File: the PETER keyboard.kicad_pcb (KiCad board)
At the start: 2 copper layers, 241.6 x 96.9 mm, 141 parts, among them J1 USB_C_Receptacle_USB2.0, SW1 RotaryEncoder_Switch, SW12 RotaryEncoder_Switch, SW2 SW_Push, U1 ATmega32U4-M, Y1 Crystal_GND24_Small

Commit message: re doing the auto routing
having to start again
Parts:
- moved C_Decoupler3 4.07 mm to (154.7, 98.7)
- moved U1 1.37 mm to (150.2, 104.3), turned to 45 degrees
- moved C_Decoupler1 0.28 mm to (145.8, 96.9)
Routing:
- net GND: track 430.5 -> 0.00 mm
- net ROW0: track 309.4 -> 0.00 mm
- net ROW2: track 255.9 -> 0.00 mm, vias 2 -> 0
- net ROTARY_A: track 242.3 -> 0.00 mm
- net ROTARY_B: track 237.0 -> 0.00 mm
- net ROW4: track 217.1 -> 0.00 mm
- net ROW1: track 216.5 -> 0.00 mm, vias 2 -> 0
- net  ROW3: track 215.9 -> 0.00 mm
- net +5V: track 91.5 -> 0.00 mm
- net COL7: track 90.7 -> 0.00 mm
- net COL0: track 90.0 -> 0.00 mm
- net COL5: track 86.5 -> 0.00 mm
- net COL1: track 84.1 -> 0.00 mm
- net COL4: track 83.1 -> 0.00 mm
- net COL2: track 83.1 -> 0.00 mm
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
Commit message: back to autorouting
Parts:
- moved U1 0.46 mm to (149.9, 104.5), turned to 0 degrees
- moved C_Decoupler3 0.28 mm to (154.9, 98.6)
- turned C_Decoupler2 to 180 degrees
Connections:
- U1 pad 10: unconnected-(U1-Pad10) -> ROW2
- U1 pad 11: unconnected-(U1-Pad11) -> COL0
- U1 pad 12: unconnected-(U1-Pad12) -> COL1
- U1 pad 18: unconnected-(U1-Pad18) -> COL2
- U1 pad 19: unconnected-(U1-Pad19) -> COL3
- U1 pad 20: unconnected-(U1-Pad20) -> COL4
- U1 pad 21: unconnected-(U1-Pad21) -> COL5
- U1 pad 22: unconnected-(U1-Pad22) -> COL6
- U1 pad 25: unconnected-(U1-Pad25) -> COL7
- U1 pad 26: unconnected-(U1-Pad26) -> COL8
- U1 pad 27: unconnected-(U1-Pad27) -> COL9
- U1 pad 31: unconnected-(U1-Pad31) -> ROTARY_A
- U1 pad 32: unconnected-(U1-Pad32) -> ROTARY_B
- U1 pad 38: unconnected-(U1-Pad38) -> COL10
- U1 pad 39: unconnected-(U1-Pad39) -> COL11
- U1 pad 40: unconnected-(U1-Pad40) -> ROW4
- U1 pad 41: unconnected-(U1-Pad41) ->  ROW3
- U1 pad 8: unconnected-(U1-Pad8) -> ROW0
- U1 pad 9: unconnected-(U1-Pad9) -> ROW1
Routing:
- added copper zone on B.Cu, net GND
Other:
- board text added: "add the pcb cut outs for bottom mounting"

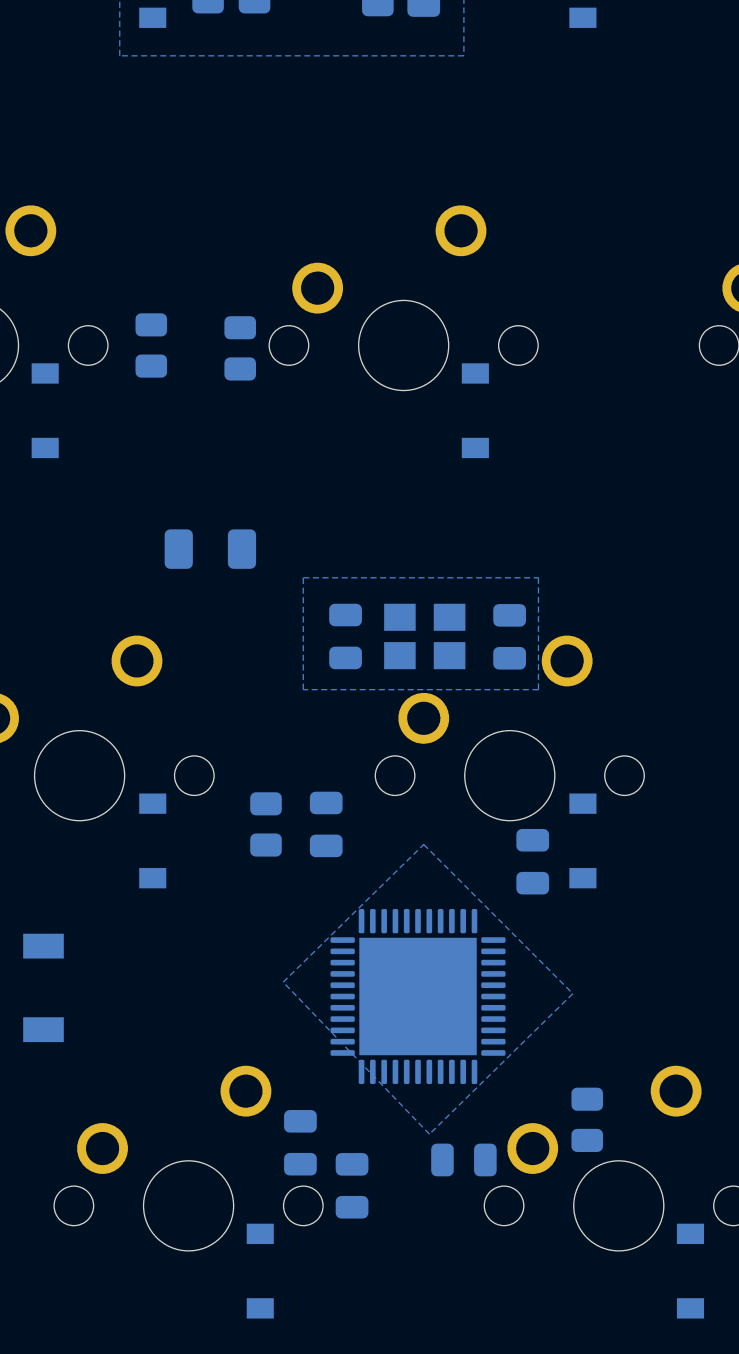
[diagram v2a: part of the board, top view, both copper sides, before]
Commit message: moving MCU around, no trace attempt yet
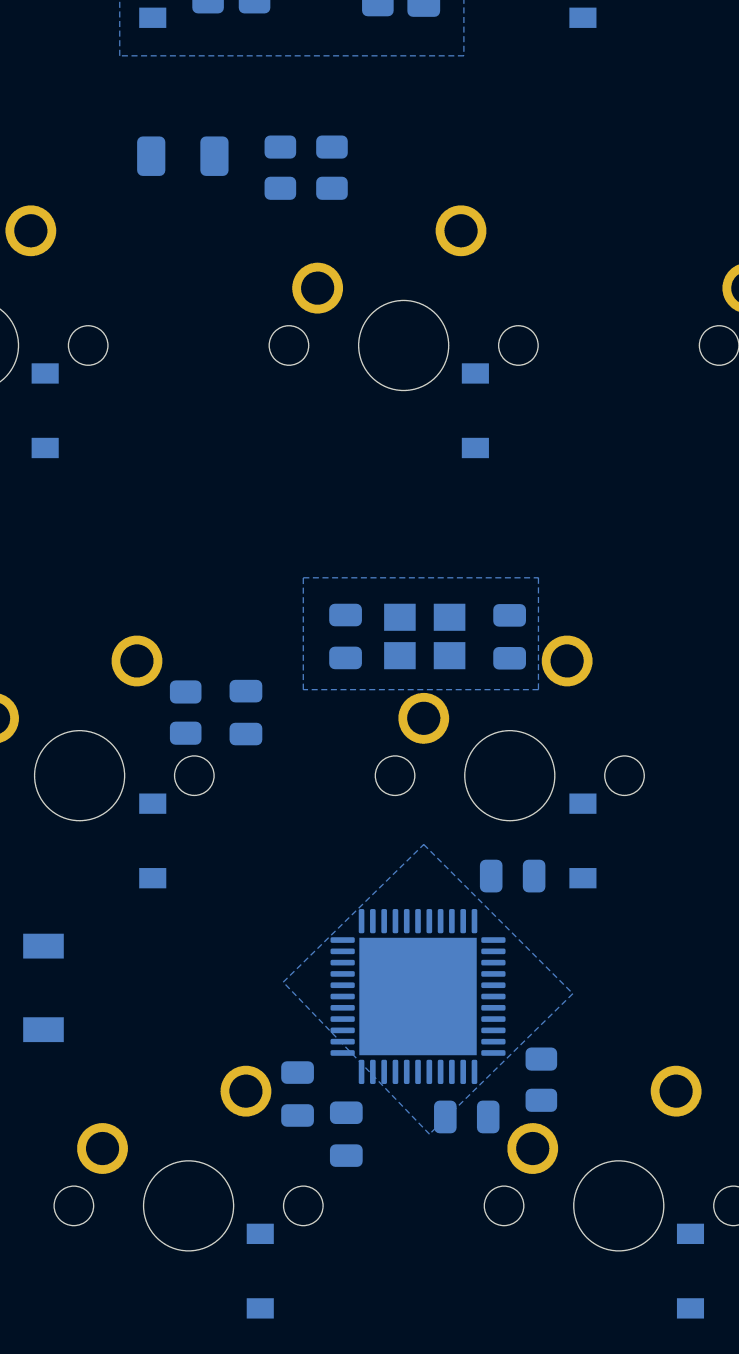
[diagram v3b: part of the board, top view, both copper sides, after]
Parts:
- moved F_USBC1 17.4 mm to (139.4, 67.3)
- moved R_USB3 9.73 mm to (143.8, 67.8)
- moved R_USB4 8.97 mm to (146.1, 67.8)
- moved C_Decoupler1 6.10 mm to (142.2, 91.9)
- moved R_reset1 6.10 mm to (139.6, 91.9)
- moved R_HWB/PE2 2.70 mm to (155.3, 108.2)
- moved C_Decoupler4 2.30 mm to (146.7, 110.6)
- moved C_UCAP1 2.16 mm to (144.5, 108.8)
- moved C_Decoupler2 1.91 mm to (152.0, 109.9)
- moved C_Decoupler3 1.09 mm to (154.1, 99.2), turned to 180 degrees
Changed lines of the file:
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@@
   )
   (footprint "Resistor_SMD:R_0805_2012Metric" (layer "B.Cu")
-    (at 143.129 96.901 -90)
+    (at 139.573 91.948 -90)
     (descr "Resistor SMD 0805 (2012 Metric), square (rectangular) end terminal, IPC_7351 nominal, (Body size source: IPC-SM-782 page 72, https://www.pcb-3d.com/wordpress/wp-content/uploads/ipc-sm-782a_amendment_1_and_2.pdf), generated with kicad-footprint-generator")
     (tags "resistor")
@@
   )
   (footprint "Resistor_SMD:R_0805_2012Metric" (layer "B.Cu")
-    (at 157.353 109.982 -90)
+    (at 155.321 108.204 -90)
     (descr "Resistor SMD 0805 (2012 Metric), square (rectangular) end terminal, IPC_7351 nominal, (Body size source: IPC-SM-782 page 72, https://www.pcb-3d.com/wordpress/wp-content/uploads/ipc-sm-782a_amendment_1_and_2.pdf), generated with kicad-footprint-generator")
     (tags "resistor")
@@
   )
   (footprint "Capacitor_SMD:C_0805_2012Metric" (layer "B.Cu")
-    (at 145.796 96.901 90)
+    (at 142.24 91.948 90)
     (descr "Capacitor SMD 0805 (2012 Metric), square (rectangular) end terminal, IPC_7351 nominal, (Body size source: IPC-SM-782 page 76, https://www.pcb-3d.com/wordpress/wp-content/uploads/ipc-sm-782a_amendment_1_and_2.pdf, https://docs.google.com/spreadsheets/d/1BsfQQcO9C6DZCsRaXUlFlo91Tg2WpOkGARC1WS5S8t0/edit?usp=sharing), generated with kicad-footprint-generator")
     (tags "capacitor")
@@
   )
   (footprint "Resistor_SMD:R_0805_2012Metric" (layer "B.Cu")
-    (at 138.049 75.692 -90)
+    (at 143.764 67.818 -90)
     (descr "Resistor SMD 0805 (2012 Metric), square (rectangular) end terminal, IPC_7351 nominal, (Body size source: IPC-SM-782 page 72, https://www.pcb-3d.com/wordpress/wp-content/uploads/ipc-sm-782a_amendment_1_and_2.pdf), generated with kicad-footprint-generator")
     (tags "resistor")
@@
   )
   (footprint "Capacitor_SMD:C_0805_2012Metric" (layer "B.Cu")
-    (at 151.892 111.76 180)
+    (at 152.019 109.855 180)
     (descr "Capacitor SMD 0805 (2012 Metric), square (rectangular) end terminal, IPC_7351 nominal, (Body size source: IPC-SM-782 page 76, https://www.pcb-3d.com/wordpress/wp-content/uploads/ipc-sm-782a_amendment_1_and_2.pdf, https://docs.google.com/spreadsheets/d/1BsfQQcO9C6DZCsRaXUlFlo91Tg2WpOkGARC1WS5S8t0/edit?usp=sharing), generated with kicad-footprint-generator")
     (tags "capacitor")
@@
   )
   (footprint "Resistor_SMD:R_0805_2012Metric" (layer "B.Cu")
-    (at 141.986 75.819 -90)
+    (at 146.05 67.818 -90)
     (descr "Resistor SMD 0805 (2012 Metric), square (rectangular) end terminal, IPC_7351 nominal, (Body size source: IPC-SM-782 page 72, https://www.pcb-3d.com/wordpress/wp-content/uploads/ipc-sm-782a_amendment_1_and_2.pdf), generated with kicad-footprint-generator")
     (tags "resistor")
@@
   )
   (footprint "Fuse:Fuse_1206_3216Metric" (layer "B.Cu")
-    (at 140.6652 84.709 180)
+    (at 139.446 67.31 180)
     (descr "Fuse SMD 1206 (3216 Metric), square (rectangular) end terminal, IPC_7351 nominal, (Body size source: http://www.tortai-tech.com/upload/download/2011102023233369053.pdf), generated with kicad-footprint-generator")
     (tags "fuse")
@@
   )
   (footprint "Capacitor_SMD:C_0805_2012Metric" (layer "B.Cu")
-    (at 144.653 110.998 -90)
+    (at 144.526 108.839 -90)
     (descr "Capacitor SMD 0805 (2012 Metric), square (rectangular) end terminal, IPC_7351 nominal, (Body size source: IPC-SM-782 page 76, https://www.pcb-3d.com/wordpress/wp-content/uploads/ipc-sm-782a_amendment_1_and_2.pdf, https://docs.google.com/spreadsheets/d/1BsfQQcO9C6DZCsRaXUlFlo91Tg2WpOkGARC1WS5S8t0/edit?usp=sharing), generated with kicad-footprint-generator")
     (tags "capacitor")
@@
   )
   (footprint "Capacitor_SMD:C_0805_2012Metric" (layer "B.Cu")
-    (at 146.939 112.903 -90)
+    (at 146.685 110.617 -90)
     (descr "Capacitor SMD 0805 (2012 Metric), square (rectangular) end terminal, IPC_7351 nominal, (Body size source: IPC-SM-782 page 76, https://www.pcb-3d.com/wordpress/wp-content/uploads/ipc-sm-782a_amendment_1_and_2.pdf, https://docs.google.com/spreadsheets/d/1BsfQQcO9C6DZCsRaXUlFlo91Tg2WpOkGARC1WS5S8t0/edit?usp=sharing), generated with kicad-footprint-generator")
     (tags "capacitor")
@@
   )
   (footprint "Capacitor_SMD:C_0805_2012Metric" (layer "B.Cu")
-    (at 154.94 98.552 90)
+    (at 154.051 99.187 180)
     (descr "Capacitor SMD 0805 (2012 Metric), square (rectangular) end terminal, IPC_7351 nominal, (Body size source: IPC-SM-782 page 76, https://www.pcb-3d.com/wordpress/wp-content/uploads/ipc-sm-782a_amendment_1_and_2.pdf, https://docs.google.com/spreadsheets/d/1BsfQQcO9C6DZCsRaXUlFlo91Tg2WpOkGARC1WS5S8t0/edit?usp=sharing), generated with kicad-footprint-generator")
     (tags "capacitor")
@@
     (property "Sheetname" "")
     (attr smd)
-    (fp_text reference "C_Decoupler3" (at 0 1.68 90) (layer "B.SilkS") hide
-      (effects (font (size 1 1) (thickness 0.15)) (justify mirror))
-    )
-    (fp_text value "0.1uF" (at 0 -1.68 90) (layer "B.Fab")
-      (effects (font (size 1 1) (thickness 0.15)) (justify mirror))
-    )
-    (fp_text user "${REFERENCE}" (at 0 0 90) (layer "B.Fab")
+    (fp_text reference "C_Decoupler3" (at 0 1.68) (layer "B.SilkS") hide
+      (effects (font (size 1 1) (thickness 0.15)) (justify mirror))
+    )
+    (fp_text value "0.1uF" (at 0 -1.68) (layer "B.Fab")
+      (effects (font (size 1 1) (thickness 0.15)) (justify mirror))
+    )
+    (fp_text user "${REFERENCE}" (at 0 0) (layer "B.Fab")
       (effects (font (size 0.5 0.5) (thickness 0.08)) (justify mirror))
     )
@@
     (fp_line (start 1 0.625) (end 1 -0.625) (layer "B.Fab") (width 0.1))
     (fp_line (start 1 -0.625) (end -1 -0.625) (layer "B.Fab") (width 0.1))
-    (pad "1" smd roundrect (at -0.95 0 90) (size 1 1.45) (layers "B.Cu" "B.Paste" "B.Mask") (roundrect_rratio 0.25)
+    (pad "1" smd roundrect (at -0.95 0 180) (size 1 1.45) (layers "B.Cu" "B.Paste" "B.Mask") (roundrect_rratio 0.25)
       (net 4 "+5V") (pintype "passive"))
-    (pad "2" smd roundrect (at 0.95 0 90) (size 1 1.45) (layers "B.Cu" "B.Paste" "B.Mask") (roundrect_rratio 0.25)
+    (pad "2" smd roundrect (at 0.95 0 180) (size 1 1.45) (layers "B.Cu" "B.Paste" "B.Mask") (roundrect_rratio 0.25)
       (net 1 "GND") (pintype "passive"))
     (model "${KICAD6_3DMODEL_DIR}/Capacitor_SMD.3dshapes/C_0805_2012Metric.wrl"

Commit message: just tried and deleted a silkscreen
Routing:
- removed copper zone on B.Cu, net GND
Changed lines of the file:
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@@
     (style (thickness 0.15) (arrow_length 1.27) (text_position_mode 0) (extension_height 0.58642) (extension_offset 0.5) keep_text_aligned)
   )
-  (zone (net 1) (net_name "GND") (layer "B.Cu") (hatch edge 0.508)
-    (connect_pads (clearance 0.508))
-    (min_thickness 0.254) (filled_areas_thickness no)
-    (fill yes (thermal_gap 0.508) (thermal_bridge_width 0.508))
-    (polygon
-      (pts
-        (xy 151.892 47.117)
-        (xy 151.892 62.865)
-        (xy 136.652 62.865)
-        (xy 136.652 46.99)
-      )
-    )
-  )
-  (zone (net 1) (net_name "GND") (layer "B.Cu") (hatch edge 0.508)
-    (connect_pads (clearance 0.508))
-    (min_thickness 0.254) (filled_areas_thickness no)
-    (fill yes (thermal_gap 0.508) (thermal_bridge_width 0.508))
-    (polygon
-      (pts
-        (xy 156.718 104.394)
-        (xy 150.368 110.617)
-        (xy 143.891 103.886)
-        (xy 150.114 97.79)
-      )
-    )
-  )
-  (zone (net 1) (net_name "GND") (layer "B.Cu") (hatch edge 0.508)
-    (connect_pads (clearance 0.508))
-    (min_thickness 0.254) (filled_areas_thickness no)
-    (fill yes (thermal_gap 0.508) (thermal_bridge_width 0.508))
-    (polygon
-      (pts
-        (xy 155.194 90.932)
-        (xy 144.78 90.932)
-        (xy 144.78 85.979)
-        (xy 155.194 85.979)
-      )
-    )
-  )
 )

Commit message: reworking pcb placement according to schematics
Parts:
- removed D_SW1, D_SW12: D_Small, Diode_SMD:D_SOD-123
- C_Decoupler1, C_Decoupler2, C_Decoupler3, C_Decoupler4, C_UCAP1, C_USBSHIELD1, C_crystal1, C_crystal2: footprint Capacitor_SMD:C_0805_2012Metric -> Capacitor_SMD:C_0402_1005Metric
- D1, D10, D11, D12, D13, D14, D15, D16, D17, D18, D19, D2, D20, D21, D22, D23, D24, D25, D26, D27, D28, D29, D3, D30, D31, D32, D33, D34, D35, D36, D37, D38, D39, D4, D40, D41, D42, D43, D44, D45, D46, D47, D48, D49, D5, D50, D51, D52, D53, D54, D55, D56, D57, D58, D6, D7, D8, D9: footprint Diode_SMD:D_SOD-123 -> Diode_SMD:D_SOD-123F
- R_HWB/PE2, R_USB1, R_USB2, R_USB3, R_USB4, R_USBSHIELD1, R_reset1: footprint Resistor_SMD:R_0805_2012Metric -> Resistor_SMD:R_0402_1005Metric
- moved SW2 29.0 mm to (137.0, 132.3), turned to 0 degrees
- moved R_reset1 17.1 mm to (137.2, 108.8)
- moved C_Decoupler1 16.9 mm to (140.1, 108.7)
- moved C_Decoupler3 12.9 mm to (145.0, 108.5)
- moved R_HWB/PE2 10.4 mm to (145.0, 109.7), turned to 180 degrees
- moved Y1 10.3 mm to (152.7, 98.6)
- moved C_crystal2 9.96 mm to (149.7, 98.0)
- moved C_crystal1 9.70 mm to (155.4, 98.2)
- moved C_UCAP1 9.63 mm to (145.9, 99.3), turned to -135 degrees
- moved C_Decoupler4 9.58 mm to (145.7, 120.1), turned to 180 degrees
- moved F_USBC1 6.87 mm to (146.1, 65.4)
- moved R_USBSHIELD1 6.65 mm to (141.6, 58.2), turned to 90 degrees
- moved R_USB2 5.75 mm to (146.7, 55.5)
- moved R_USB1 4.27 mm to (141.9, 55.5)
- moved R_USB4 4.19 mm to (142.6, 65.4)
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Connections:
- SW1 pad S1: Net-(D_SW1-Pad2) -> Net-(D1-Pad2)
- SW12 pad S1: Net-(D_SW12-Pad2) -> Net-(D12-Pad2)
- U1 pad 10: ROW2 -> unconnected-(U1-Pad10)
- U1 pad 11: COL0 -> unconnected-(U1-Pad11)
- U1 pad 12: COL1 -> unconnected-(U1-Pad12)
- U1 pad 18: COL2 -> unconnected-(U1-Pad18)
- U1 pad 19: COL3 -> unconnected-(U1-Pad19)
- U1 pad 20: COL4 -> unconnected-(U1-Pad20)
- U1 pad 21: COL5 -> unconnected-(U1-Pad21)
- U1 pad 22: COL6 -> unconnected-(U1-Pad22)
- U1 pad 25: COL7 -> unconnected-(U1-Pad25)
- U1 pad 26: COL8 -> unconnected-(U1-Pad26)
- U1 pad 27: COL9 -> unconnected-(U1-Pad27)
- U1 pad 31: ROTARY_A -> unconnected-(U1-Pad31)
- U1 pad 32: ROTARY_B -> unconnected-(U1-Pad32)
- U1 pad 38: COL10 -> unconnected-(U1-Pad38)
- U1 pad 39: COL11 -> unconnected-(U1-Pad39)
- U1 pad 40: ROW4 -> unconnected-(U1-Pad40)
- U1 pad 41:  ROW3 -> unconnected-(U1-Pad41)
- U1 pad 8: ROW0 -> unconnected-(U1-Pad8)
- U1 pad 9: ROW1 -> unconnected-(U1-Pad9)
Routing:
- net COL11: track 0.00 -> 91.0 mm
- net COL0: track 0.00 -> 90.0 mm
- net COL7: track 0.00 -> 87.0 mm
- net COL5: track 0.00 -> 86.0 mm
- net COL1: track 0.00 -> 84.1 mm
- net COL4: track 0.00 -> 83.1 mm
- net COL2: track 0.00 -> 83.1 mm
- net COL9: track 0.00 -> 82.1 mm
- net COL8: track 0.00 -> 82.1 mm
- net COL10: track 0.00 -> 82.1 mm
- net COL6: track 0.00 -> 63.0 mm
- net COL3: track 0.00 -> 63.0 mm

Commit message: manual routing
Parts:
- moved SW2 47.4 mm to (136.1, 85.0)
- moved R_reset1 14.6 mm to (147.3, 98.3)
- moved R_HWB/PE2 12.1 mm to (157.1, 108.6), turned to -90 degrees
- moved C_Decoupler4 8.79 mm to (145.0, 111.4)
- moved C_Decoupler2 8.01 mm to (145.0, 110.4)
- moved C_UCAP1 6.61 mm to (145.5, 105.9), turned to -90 degrees
- moved C_Decoupler1 4.97 mm to (145.0, 108.3), turned to 180 degrees
- moved U1 2.67 mm to (152.1, 105.4), turned to 0 degrees
- moved C_Decoupler3 0.89 mm to (145.0, 109.3)
- moved C_crystal2 0.65 mm to (149.1, 98.2)
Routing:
- net ROW2: track 0.00 -> 94.9 mm
- net GND: track 0.00 -> 44.3 mm
- net Net-(D12-Pad2): track 0.00 -> 30.2 mm
- net Net-(R_reset1-Pad2): track 0.00 -> 26.8 mm, vias 0 -> 2
- net VCC: track 0.00 -> 20.9 mm, vias 0 -> 2
- net +5V: track 0.00 -> 16.8 mm
- net Net-(D1-Pad2): track 0.00 -> 12.4 mm
- net Net-(C_USBSHIELD1-Pad1): track 0.00 -> 11.2 mm, vias 0 -> 1
- net Net-(R_USB3-Pad2): track 0.00 -> 9.86 mm, vias 0 -> 1
- net Net-(C_crystal2-Pad2): track 0.00 -> 8.42 mm
- net Net-(D23-Pad2): track 0.00 -> 8.01 mm
- net Net-(R_USB4-Pad2): track 0.00 -> 7.55 mm, vias 0 -> 1
- net Net-(D49-Pad2): track 0.00 -> 6.87 mm
- net Net-(D25-Pad2): track 0.00 -> 6.87 mm
- net Net-(D51-Pad2): track 0.00 -> 6.86 mm
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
